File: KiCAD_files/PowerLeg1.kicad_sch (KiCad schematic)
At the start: 72 parts, among them J1 Conn_01x01, J10 Conn_01x01, J2 Conn_01x01, J3 Conn_01x01, J4 Conn_01x01, J5 Conn_01x01, J6 Conn_01x01, J7 Conn_01x01, J8 Conn_01x01, J9 Conn_01x01, Q1 IPD200N15N3, Q2 IPD200N15N3, Q3 IPD200N15N3, U1 AMC1100DUB, U2 ACS730xLCTR-20AB, U3 UCC21222DR, U4 OPA316, U5 OPA316, U6 SFH617A-2X009T

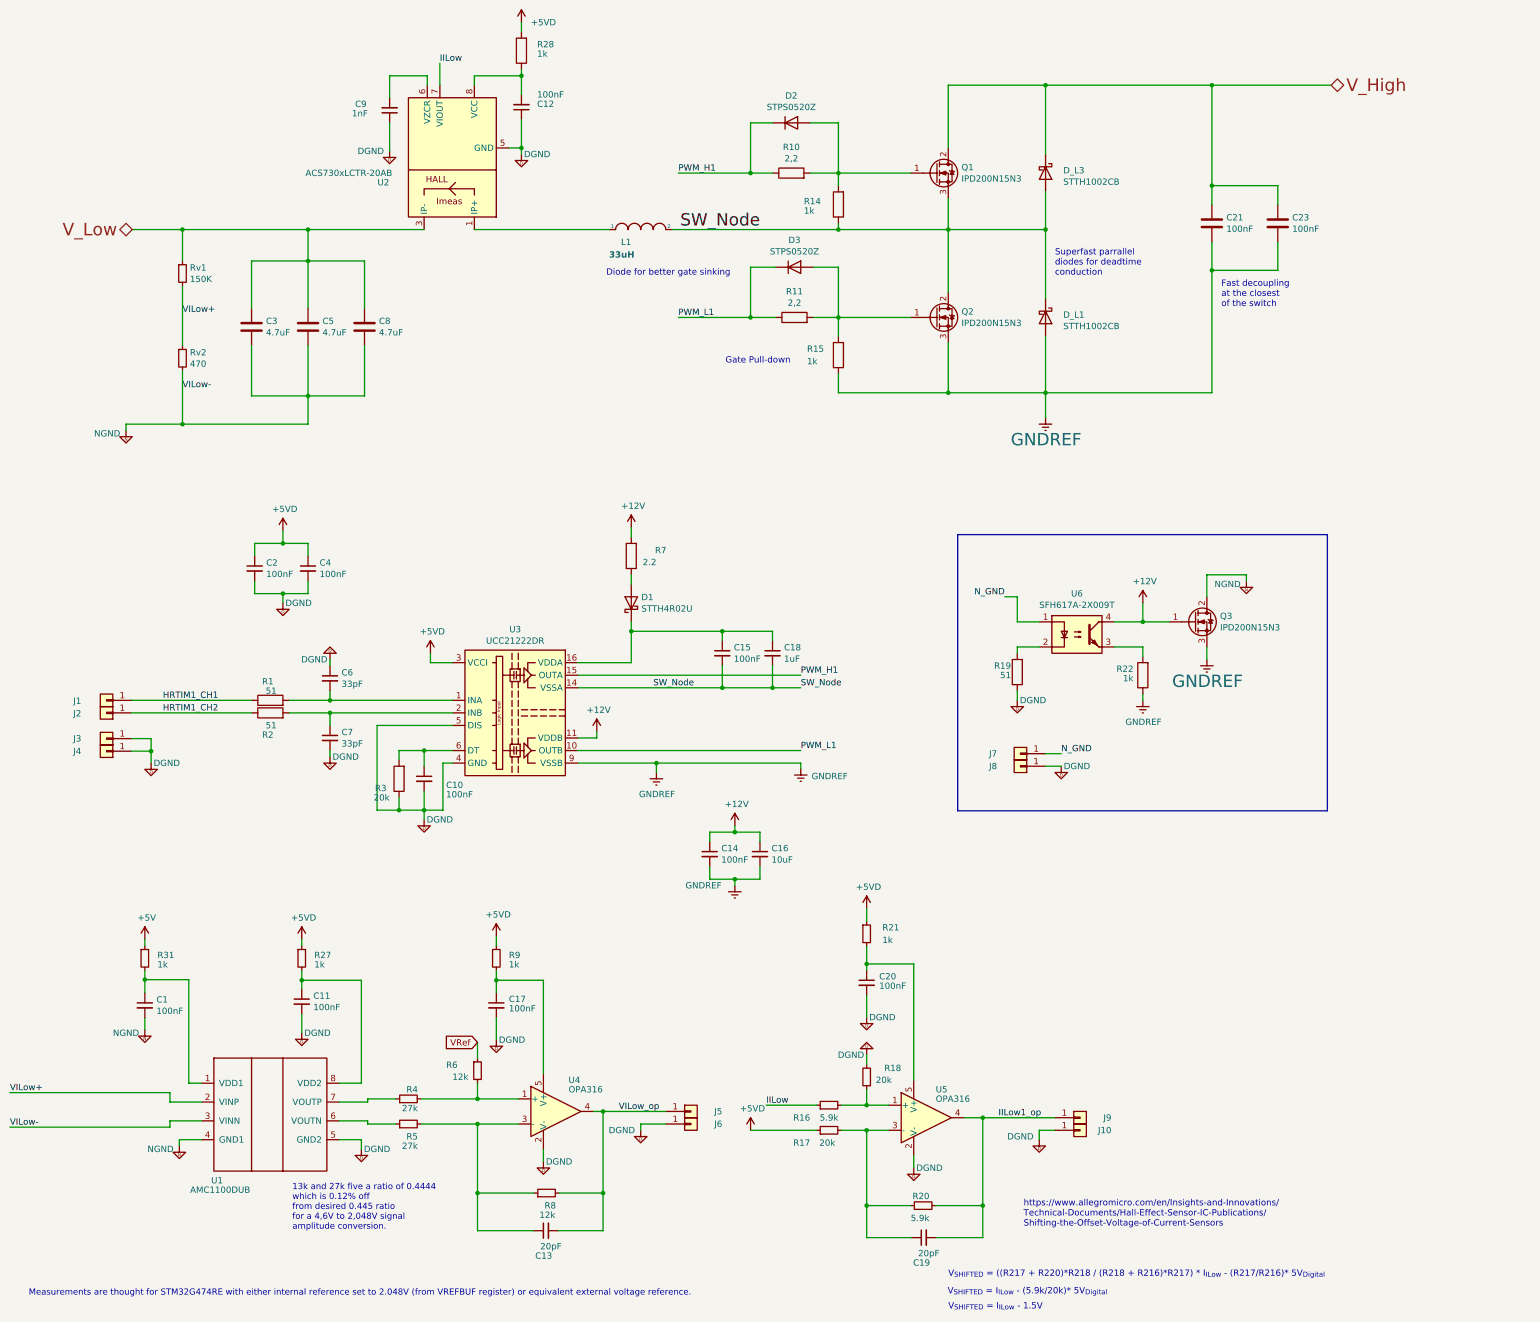
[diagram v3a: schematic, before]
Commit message: WIP: mooving to a single board implementation with 160x100 form factor.
Former-commit-id: e8c19d5fc5237412fb5a003591d44756dbc6e173
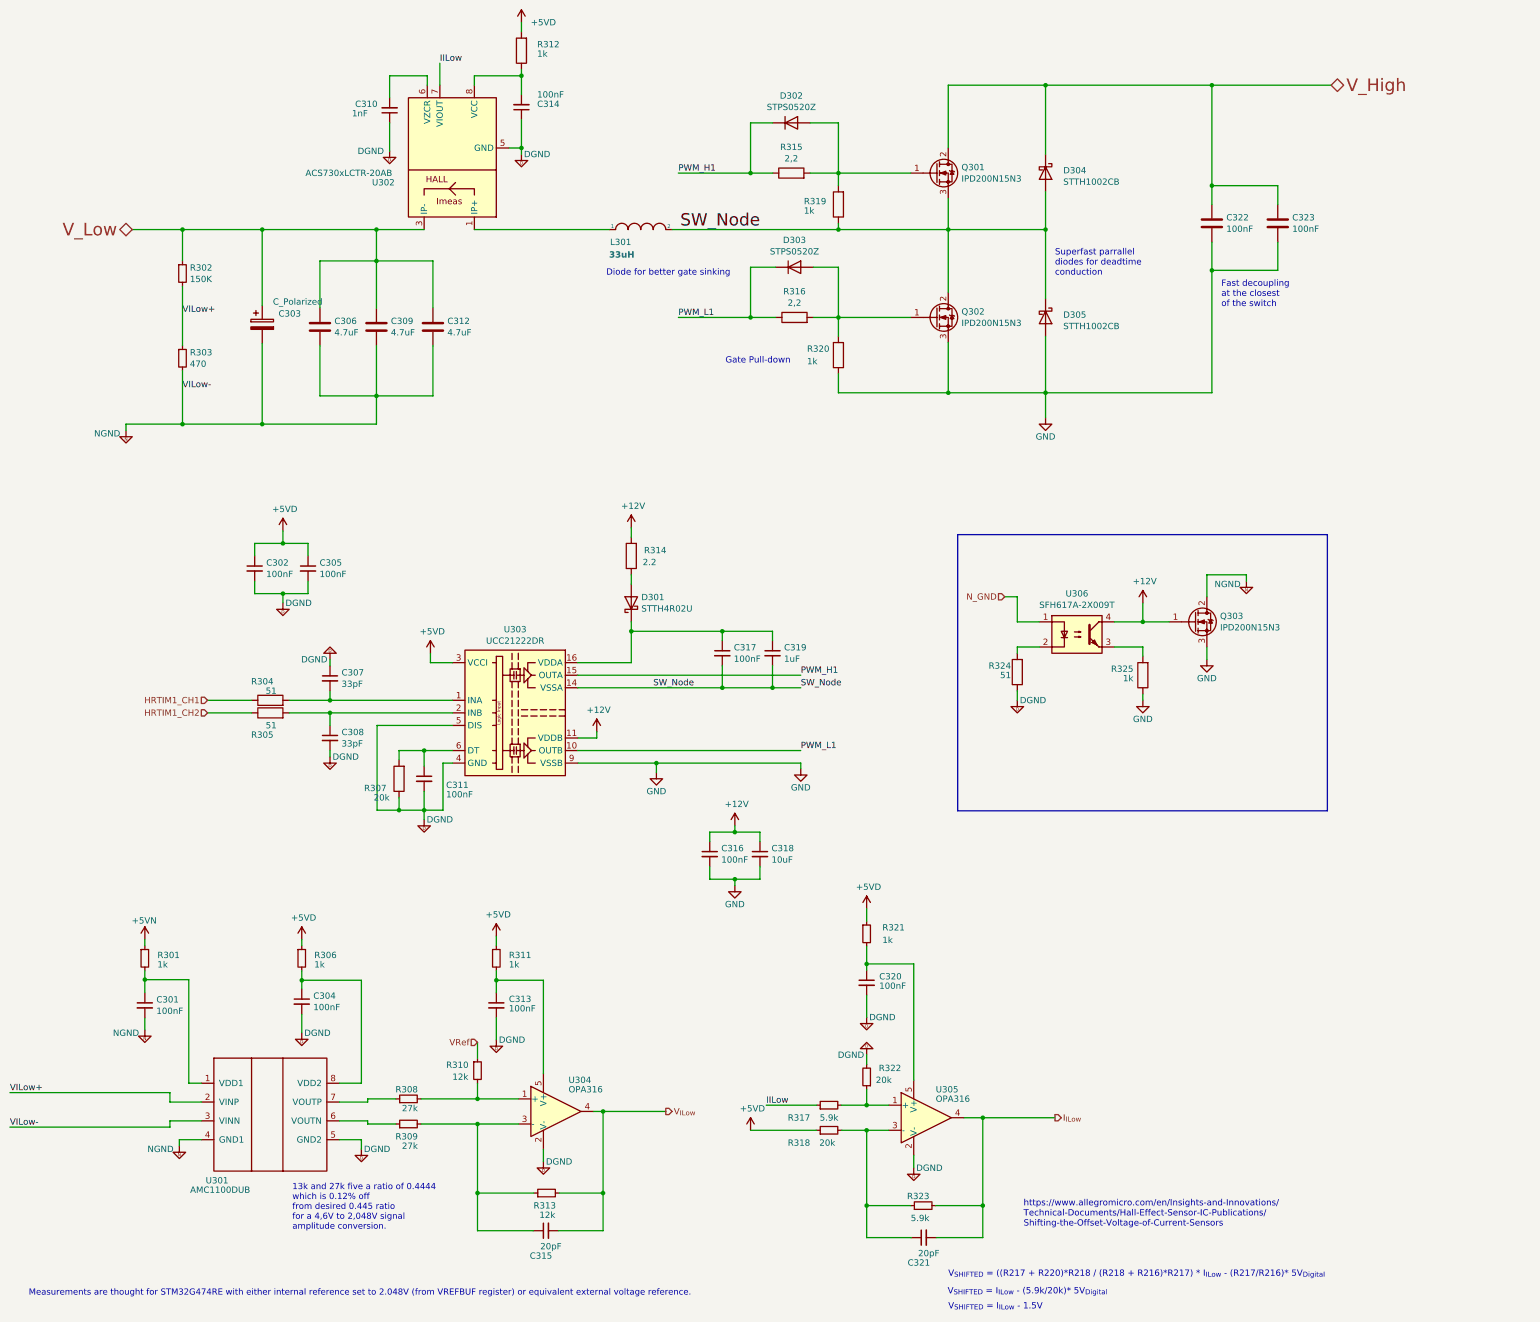
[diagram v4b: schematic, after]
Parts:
- removed J1, J10, J2, J3, J4, J5, J6, J7, J8, J9: Conn_01x01, Footprints:0906_millmax, symbol Connector_Generic:Conn_01x01
- added C303: C_Polarized, Capacitor_SMD:CP_Elec_10x10.5, symbol Device:C_Polarized
- D302: renamed from D2; footprint Diode_SMD:D_SOD-123 -> Diode_SMD:D_SOD-323
- D303: renamed from D3; footprint Diode_SMD:D_SOD-123 -> Diode_SMD:D_SOD-323
- renumbered C1 to C301, C2 to C302, C11 to C304, C4 to C305, C3 to C306, C6 to C307, C7 to C308, C5 to C309, C9 to C310, C10 to C311, C8 to C312, C17 to C313, C12 to C314, C13 to C315, C14 to C316, C15 to C317, C16 to C318, C18 to C319, C20 to C320, C19 to C321, C21 to C322, C23 to C323, D1 to D301, D_L3 to D304, D_L1 to D305, L1 to L301, Q1 to Q301, Q2 to Q302, Q3 to Q303, R31 to R301, Rv1 to R302, Rv2 to R303, R1 to R304, R2 to R305, R27 to R306, R3 to R307, R4 to R308, R5 to R309, R6 to R310, R9 to R311, R28 to R312, R8 to R313, R7 to R314, R10 to R315, R11 to R316, R16 to R317, R17 to R318, R14 to R319, R15 to R320, R21 to R321, R18 to R322, R20 to R323, R19 to R324, R22 to R325, U1 to U301, U2 to U302, U3 to U303, U4 to U304, U5 to U305, U6 to U306
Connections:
- net NGND: now also C303.2
- net V_Low: now also C303.1
- net +5V renamed +5VN
- net GNDREF renamed GND
- net IILow1_op renamed I_{ILow}
- net VILow_op renamed V_{ILow}
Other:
- moved on the sheet: C306, C309, C312

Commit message: WIP : Mechanical drawings and fab drawings have been cleaned up
Former-commit-id: 134f220442ec2a3fea5dbd7da82e3ae2ef008ff9
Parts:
- C303: value C_Polarized -> 47uF; VRating (none) -> 100V
- C306, C309, C312: VRating (none) -> 100V
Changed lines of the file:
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@@
       (effects (font (size 1.27 1.27)) hide)
     )
+    (property "VRating" "100V" (id 5) (at 87.63 84.455 0))
     (pin "1")
     (pin "2")
@@
       (effects (font (size 1.27 1.27)) hide)
     )
+    (property "VRating" "100V" (id 5) (at 110.49 84.455 0))
     (pin "1")
     (pin "2")
@@
       (effects (font (size 1.27 1.27)) (justify left))
     )
-    (property "Value" "C_Polarized" (id 1) (at 72.263 76.2 0)
+    (property "Value" "47uF " (id 1) (at 73.66 80.645 0)
       (effects (font (size 1.27 1.27)) (justify left))
     )
@@
       (effects (font (size 1.27 1.27)) hide)
     )
+    (property "VRating" "100V" (id 4) (at 76.2 82.55 0))
     (pin "1")
     (pin "2")
@@
       (effects (font (size 1.27 1.27)) hide)
     )
-    (pin "1")
-    (pin "2")
+    (property "VRating" "100V" (id 5) (at 99.06 84.455 0))
+    (pin "1")
+    (pin "2")
